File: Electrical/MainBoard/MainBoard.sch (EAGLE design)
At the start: 122 parts, among them IC1 MEGA1284-P, IC2 MCP4922-E/SL, IC3 MCP4921-E/SN, IC4 TL074D, IC5 TL074D, IC6 FT232RL, Q1 BC140-10, Q2 BC160, Q3 BC140-10, Q4 BC160, Q5 BD239, Q6 BC547, Q7 BC557, Q8 16MHz, X1 FH12-45S-0.5SH, X2 22-23-2021, X3 PN61729-S

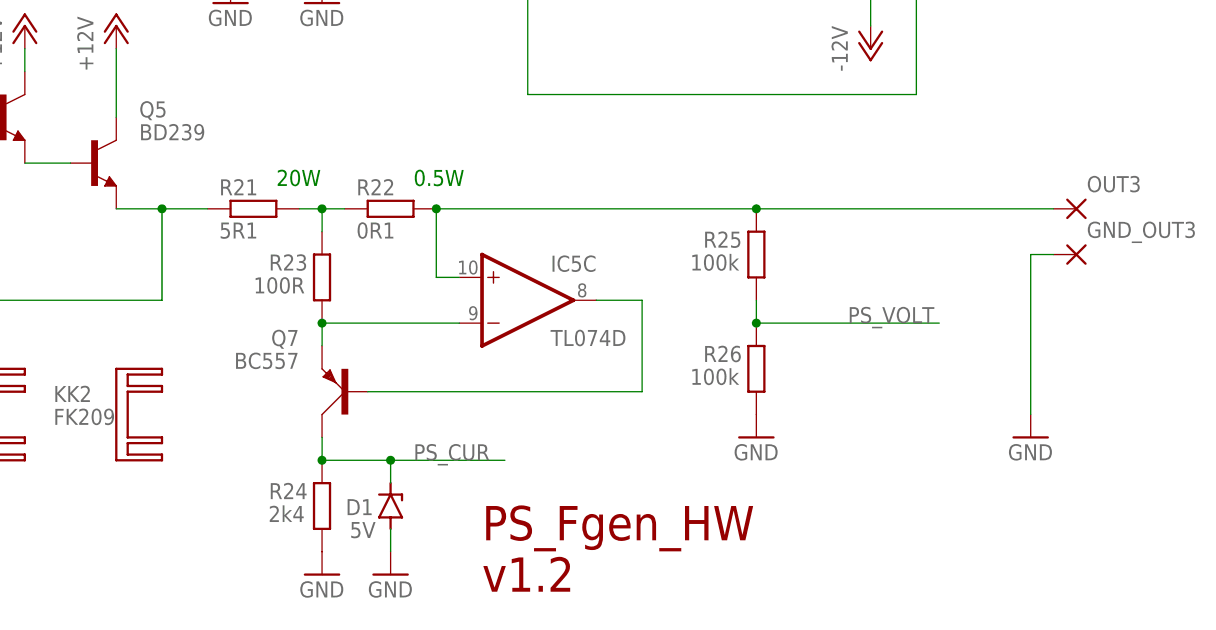
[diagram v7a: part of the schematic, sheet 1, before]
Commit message: Removed Z-Diode D1 (PS_CUR), moved resistor R21 of current measurement circuit to be after this circuit
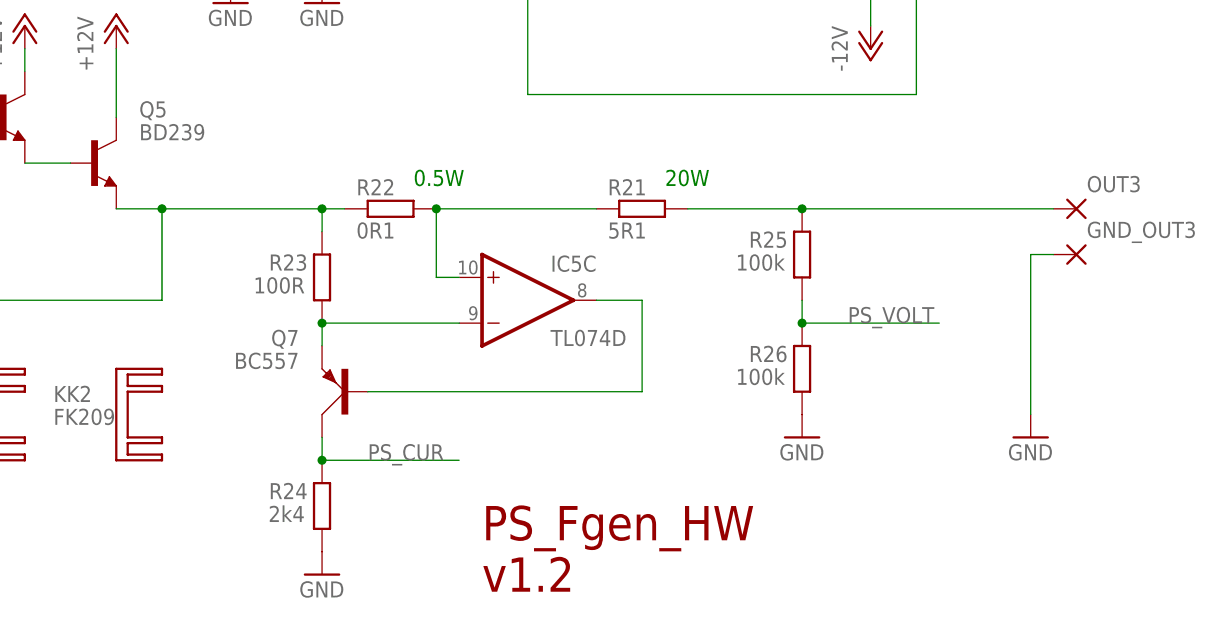
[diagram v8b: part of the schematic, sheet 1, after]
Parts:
- removed D1: 5V, diode:ZENER-DIODESOD80C
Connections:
- removed net N$21: R21.2, R22.1, R23.2
- new net N$39: IC5C.+IN, R21.1, R22.2
- net GND: no longer D1.A
- net N$18: now also R22.1, R23.2; no longer R21.1
- net N$22: now also R21.2; no longer IC5C.+IN, R22.2
- net PS_CUR: no longer D1.C
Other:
- moved on the sheet: R21, R25, R26
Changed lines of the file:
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@@
 <part name="R26" library="OwnDevices" library_urn="urn:adsk.eagle:library:19498084" deviceset="R-EU_" device="R0805" package3d_urn="urn:adsk.eagle:package:23553/2" value="100k"/>
 <part name="GND9" library="supply1" library_urn="urn:adsk.eagle:library:371" deviceset="GND" device=""/>
-<part name="D1" library="diode" library_urn="urn:adsk.eagle:library:210" deviceset="ZENER-DIODE" device="SOD80C" package3d_urn="urn:adsk.eagle:package:43405/2" value="5V"/>
-<part name="GND10" library="supply1" library_urn="urn:adsk.eagle:library:371" deviceset="GND" device=""/>
 <part name="FRAME1" library="frames" library_urn="urn:adsk.eagle:library:229" deviceset="A4L-LOC" device=""/>
 <part name="FRAME2" library="frames" library_urn="urn:adsk.eagle:library:229" deviceset="A4L-LOC" device=""/>
@@
 <text x="7.62" y="63.5" size="3.81" layer="97">Power Supply</text>
 <text x="154.94" y="58.42" size="1.778" layer="91">0.5W</text>
-<text x="139.7" y="58.42" size="1.778" layer="91">20W</text>
+<text x="182.88" y="58.42" size="1.778" layer="91">20W</text>
 </plain>
 <instances>
@@
 <attribute name="VALUE" x="119.38" y="71.12" size="1.778" layer="96" rot="R90"/>
 </instance>
-<instance part="R21" gate="G$1" x="137.16" y="55.88" smashed="yes">
-<attribute name="NAME" x="133.35" y="57.3786" size="1.778" layer="95"/>
-<attribute name="VALUE" x="133.35" y="52.578" size="1.778" layer="96"/>
+<instance part="R21" gate="G$1" x="180.34" y="55.88" smashed="yes">
+<attribute name="NAME" x="176.53" y="57.3786" size="1.778" layer="95"/>
+<attribute name="VALUE" x="176.53" y="52.578" size="1.778" layer="96"/>
 </instance>
 <instance part="R22" gate="G$1" x="152.4" y="55.88" smashed="yes">
@@
 <attribute name="VALUE" x="142.24" y="12.7" size="1.778" layer="96"/>
 </instance>
-<instance part="R25" gate="G$1" x="193.04" y="50.8" smashed="yes" rot="R90">
-<attribute name="NAME" x="191.4525" y="53.34" size="1.778" layer="95" rot="R180"/>
-<attribute name="VALUE" x="191.135" y="50.8" size="1.778" layer="96" rot="R180"/>
-</instance>
-<instance part="R26" gate="G$1" x="193.04" y="38.1" smashed="yes" rot="R90">
-<attribute name="NAME" x="191.4525" y="40.64" size="1.778" layer="95" rot="R180"/>
-<attribute name="VALUE" x="191.135" y="38.1" size="1.778" layer="96" rot="R180"/>
-</instance>
-<instance part="GND9" gate="1" x="193.04" y="30.48" smashed="yes">
-<attribute name="VALUE" x="190.5" y="27.94" size="1.778" layer="96"/>
-</instance>
-<instance part="D1" gate="G$1" x="152.4" y="22.86" smashed="yes" rot="R90">
-<attribute name="NAME" x="150.495" y="23.622" size="1.778" layer="95" rot="R180"/>
-<attribute name="VALUE" x="150.749" y="21.082" size="1.778" layer="96" rot="R180"/>
-</instance>
-<instance part="GND10" gate="1" x="152.4" y="15.24" smashed="yes">
-<attribute name="VALUE" x="149.86" y="12.7" size="1.778" layer="96"/>
+<instance part="R25" gate="G$1" x="198.12" y="50.8" smashed="yes" rot="R90">
+<attribute name="NAME" x="196.5325" y="53.34" size="1.778" layer="95" rot="R180"/>
+<attribute name="VALUE" x="196.215" y="50.8" size="1.778" layer="96" rot="R180"/>
+</instance>
+<instance part="R26" gate="G$1" x="198.12" y="38.1" smashed="yes" rot="R90">
+<attribute name="NAME" x="196.5325" y="40.64" size="1.778" layer="95" rot="R180"/>
+<attribute name="VALUE" x="196.215" y="38.1" size="1.778" layer="96" rot="R180"/>
+</instance>
+<instance part="GND9" gate="1" x="198.12" y="30.48" smashed="yes">
+<attribute name="VALUE" x="195.58" y="27.94" size="1.778" layer="96"/>
 </instance>
 <instance part="FRAME1" gate="G$1" x="0" y="0" smashed="yes">
@@
 <pinref part="R26" gate="G$1" pin="1"/>
 <pinref part="GND9" gate="1" pin="GND"/>
-</segment>
-<segment>
-<pinref part="GND10" gate="1" pin="GND"/>
-<pinref part="D1" gate="G$1" pin="A"/>
-<wire x1="152.4" y1="17.78" x2="152.4" y2="20.32" width="0.1524" layer="91"/>
 </segment>
 <segment>
@@
 <wire x1="127" y1="45.72" x2="127" y2="55.88" width="0.1524" layer="91"/>
 <wire x1="127" y1="55.88" x2="121.92" y2="55.88" width="0.1524" layer="91"/>
-<pinref part="R21" gate="G$1" pin="1"/>
-<wire x1="132.08" y1="55.88" x2="127" y2="55.88" width="0.1524" layer="91"/>
+<pinref part="R22" gate="G$1" pin="1"/>
+<pinref part="R23" gate="G$1" pin="2"/>
+<wire x1="144.78" y1="55.88" x2="147.32" y2="55.88" width="0.1524" layer="91"/>
+<wire x1="144.78" y1="53.34" x2="144.78" y2="55.88" width="0.1524" layer="91"/>
+<wire x1="127" y1="55.88" x2="144.78" y2="55.88" width="0.1524" layer="91"/>
 <junction x="127" y="55.88"/>
+<junction x="144.78" y="55.88"/>
 </segment>
 </net>
@@
 </segment>
 </net>
-<net name="N$21" class="0">
-<segment>
+<net name="N$22" class="0">
+<segment>
+<pinref part="R25" gate="G$1" pin="2"/>
+<pinref part="OUT3" gate="P" pin="P"/>
+<wire x1="226.06" y1="55.88" x2="198.12" y2="55.88" width="0.1524" layer="91"/>
 <pinref part="R21" gate="G$1" pin="2"/>
-<pinref part="R22" gate="G$1" pin="1"/>
-<wire x1="142.24" y1="55.88" x2="144.78" y2="55.88" width="0.1524" layer="91"/>
-<pinref part="R23" gate="G$1" pin="2"/>
-<wire x1="144.78" y1="55.88" x2="147.32" y2="55.88" width="0.1524" layer="91"/>
-<wire x1="144.78" y1="53.34" x2="144.78" y2="55.88" width="0.1524" layer="91"/>
-<junction x="144.78" y="55.88"/>
-</segment>
-</net>
-<net name="N$22" class="0">
-<segment>
-<pinref part="IC5" gate="C" pin="+IN"/>
-<wire x1="160.02" y1="48.26" x2="157.48" y2="48.26" width="0.1524" layer="91"/>
-<pinref part="R22" gate="G$1" pin="2"/>
-<wire x1="157.48" y1="48.26" x2="157.48" y2="55.88" width="0.1524" layer="91"/>
-<pinref part="R25" gate="G$1" pin="2"/>
-<wire x1="157.48" y1="55.88" x2="193.04" y2="55.88" width="0.1524" layer="91"/>
-<junction x="157.48" y="55.88"/>
-<pinref part="OUT3" gate="P" pin="P"/>
-<wire x1="226.06" y1="55.88" x2="193.04" y2="55.88" width="0.1524" layer="91"/>
-<junction x="193.04" y="55.88"/>
+<wire x1="185.42" y1="55.88" x2="198.12" y2="55.88" width="0.1524" layer="91"/>
+<junction x="198.12" y="55.88"/>
 </segment>
 </net>
@@
 <pinref part="R24" gate="G$1" pin="2"/>
 <wire x1="144.78" y1="30.48" x2="144.78" y2="27.94" width="0.1524" layer="91"/>
-<pinref part="D1" gate="G$1" pin="C"/>
-<wire x1="152.4" y1="25.4" x2="152.4" y2="27.94" width="0.1524" layer="91"/>
-<wire x1="152.4" y1="27.94" x2="144.78" y2="27.94" width="0.1524" layer="91"/>
 <junction x="144.78" y="27.94"/>
-<wire x1="165.1" y1="27.94" x2="152.4" y2="27.94" width="0.1524" layer="91"/>
-<junction x="152.4" y="27.94"/>
-<label x="154.94" y="27.94" size="1.778" layer="95"/>
+<wire x1="160.02" y1="27.94" x2="144.78" y2="27.94" width="0.1524" layer="91"/>
+<label x="149.86" y="27.94" size="1.778" layer="95"/>
 </segment>
 </net>
@@
 <pinref part="R25" gate="G$1" pin="1"/>
 <pinref part="R26" gate="G$1" pin="2"/>
-<wire x1="193.04" y1="45.72" x2="193.04" y2="43.18" width="0.1524" layer="91"/>
-<junction x="193.04" y="43.18"/>
-<wire x1="213.36" y1="43.18" x2="193.04" y2="43.18" width="0.1524" layer="91"/>
+<wire x1="198.12" y1="45.72" x2="198.12" y2="43.18" width="0.1524" layer="91"/>
+<junction x="198.12" y="43.18"/>
+<wire x1="213.36" y1="43.18" x2="198.12" y2="43.18" width="0.1524" layer="91"/>
 <label x="203.2" y="43.18" size="1.778" layer="95"/>
 </segment>
@@
 </segment>
 </net>
+<net name="N$39" class="0">
+<segment>
+<pinref part="R22" gate="G$1" pin="2"/>
+<pinref part="IC5" gate="C" pin="+IN"/>
+<wire x1="160.02" y1="48.26" x2="157.48" y2="48.26" width="0.1524" layer="91"/>
+<wire x1="157.48" y1="48.26" x2="157.48" y2="55.88" width="0.1524" layer="91"/>
+<pinref part="R21" gate="G$1" pin="1"/>
+<wire x1="175.26" y1="55.88" x2="157.48" y2="55.88" width="0.1524" layer="91"/>
+<junction x="157.48" y="55.88"/>
+</segment>
+</net>
